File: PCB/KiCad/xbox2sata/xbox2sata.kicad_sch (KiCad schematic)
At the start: 43 parts, among them IC1 TLV1117LV12DCYR, J1 61203921621, J2 67800-8025, J3 90151-2140, U1 88SA8052, Y1 ABLS-25.000MHZ-B4-F-T

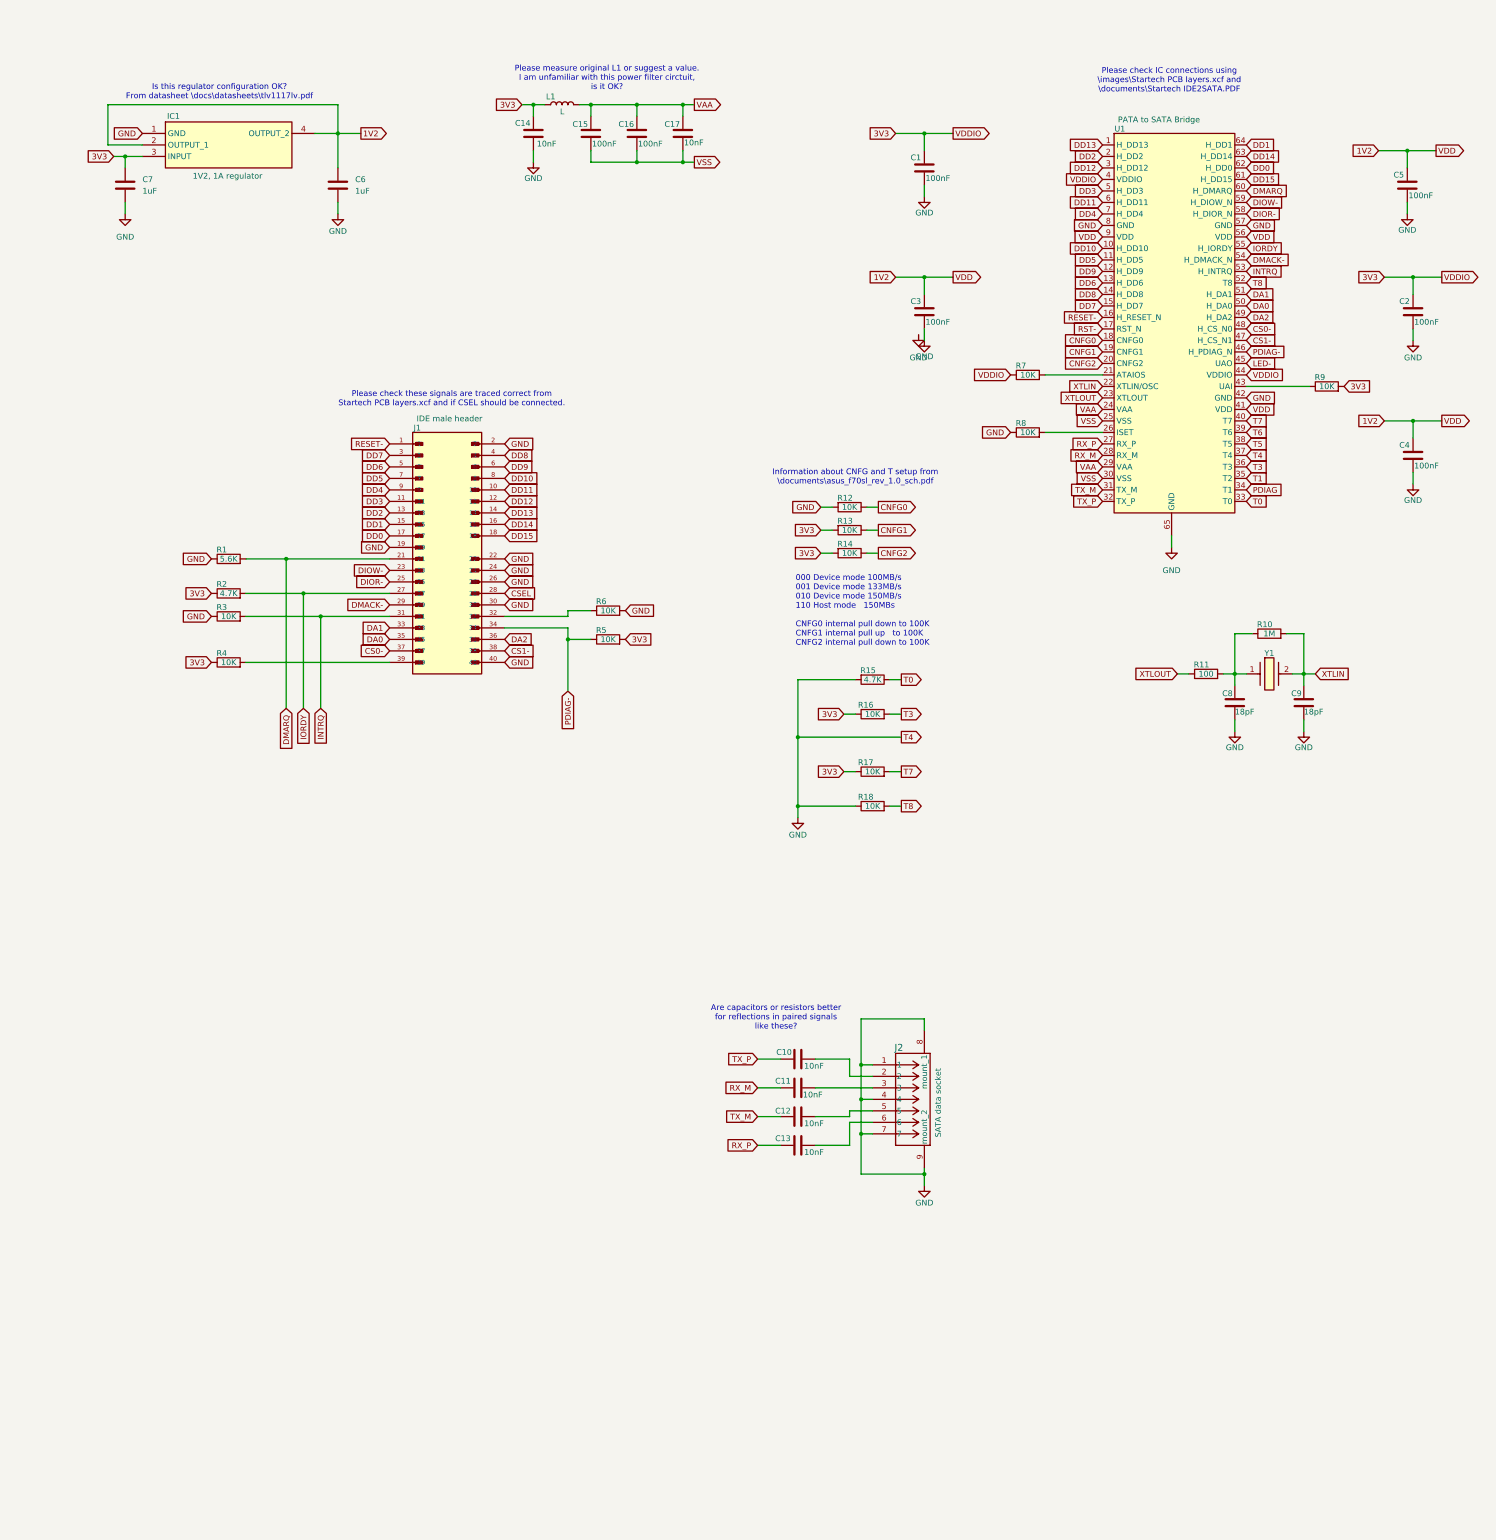
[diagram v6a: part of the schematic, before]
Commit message: 1V2 regulator circuit corrected, all labels need correcting
1V2 regulator circuit corrected, all labels need correcting
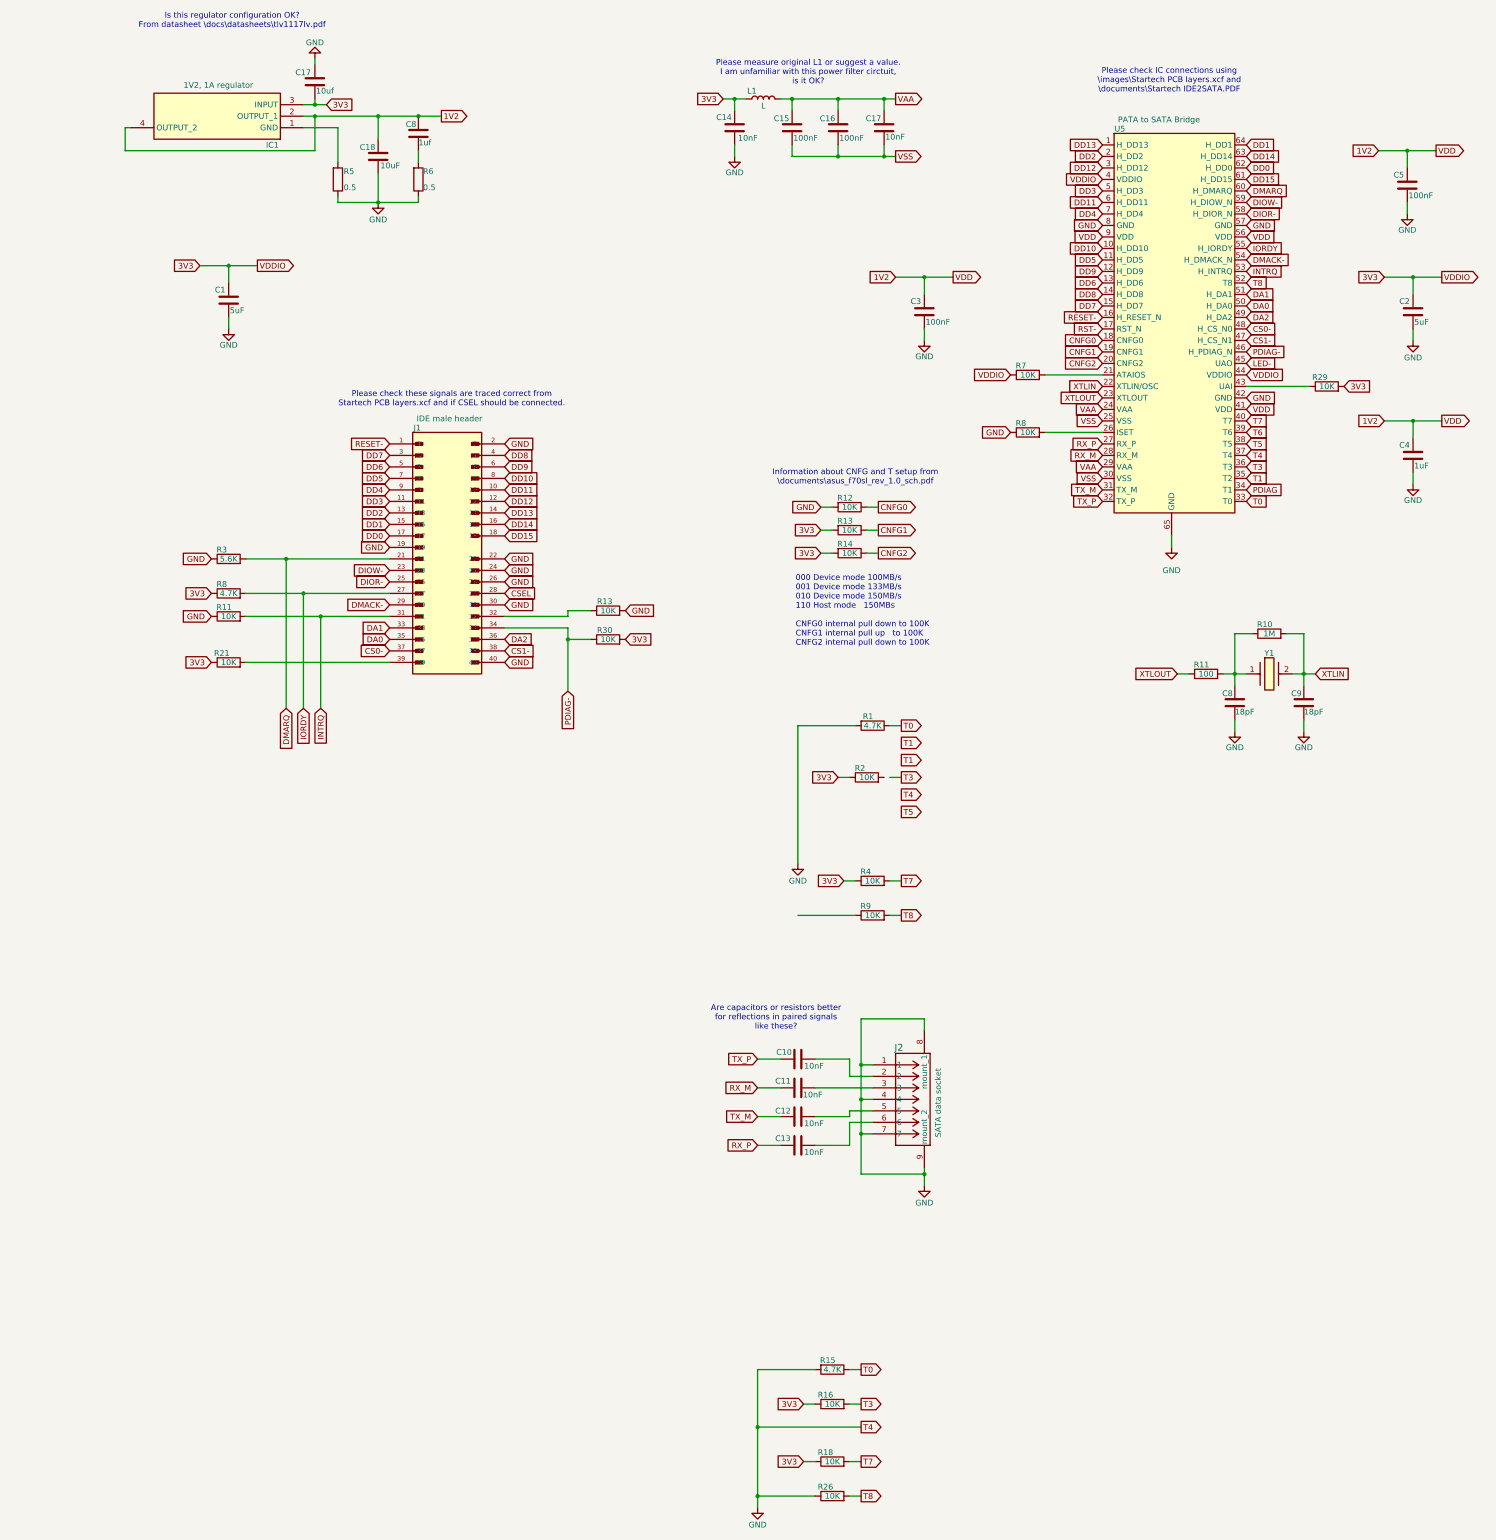
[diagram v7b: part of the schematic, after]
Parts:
- added C8: 1uf, symbol Device:C
- added R1: 4.7K, Resistor_SMD:R_0402_1005Metric_Pad0.72x0.64mm_HandSolder, symbol Device:R
- added R2, R4, R9: 10K, Resistor_SMD:R_0402_1005Metric_Pad0.72x0.64mm_HandSolder, symbol Device:R
- added R5, R6: 0.5, symbol Device:R
- C1, C2: value 100nF -> 5uF
- C17: renamed from C7; value 1uF -> 10uf
- C18: renamed from C6; value 1uF -> 10uF
- C4: value 100nF -> 1uF
- renumbered R3 to R11, R6 to R13, R17 to R18, R4 to R21, R18 to R26, R9 to R29, R1 to R3, R5 to R30, R2 to R8, U1 to U5
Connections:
- net 1V2: now also C8.2
- net 3V3: now also R2.1, R4.1
- net GND: now also R1.2, R5.1, R6.1; no longer IC1.1 (GND)
- net T0: now also R1.1
- net T7: now also R4.2
- net T8: now also R9.2
- new net: C8.1, R6.2
- new net: IC1.1 (GND), R5.2
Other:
- moved on the sheet: C1, C14, C15, C16, C17, C18, IC1, L1, R15, R16, R18, R26

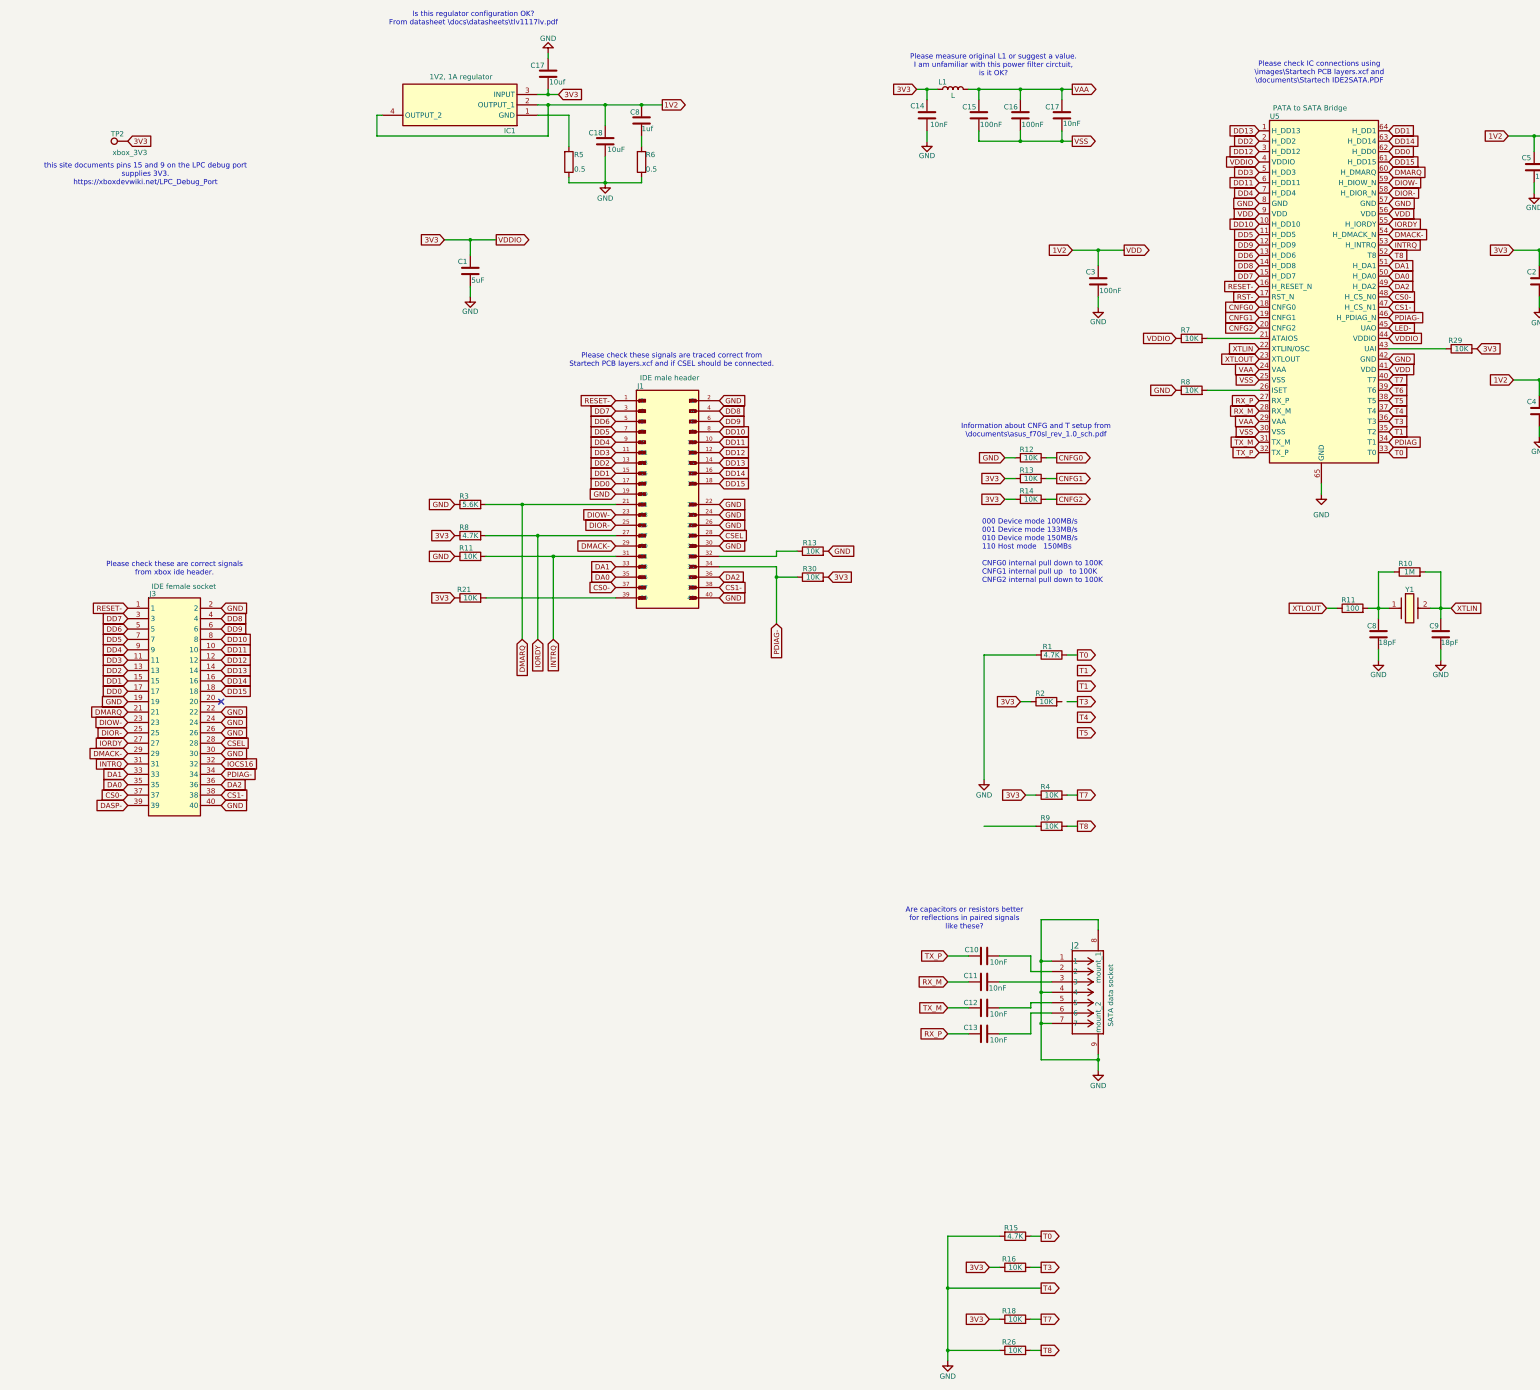
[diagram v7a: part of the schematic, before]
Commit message: T0-8 updated, label changes
Several cap and res labels changed, T0-8 config changed, layers.xcf saved with compression.
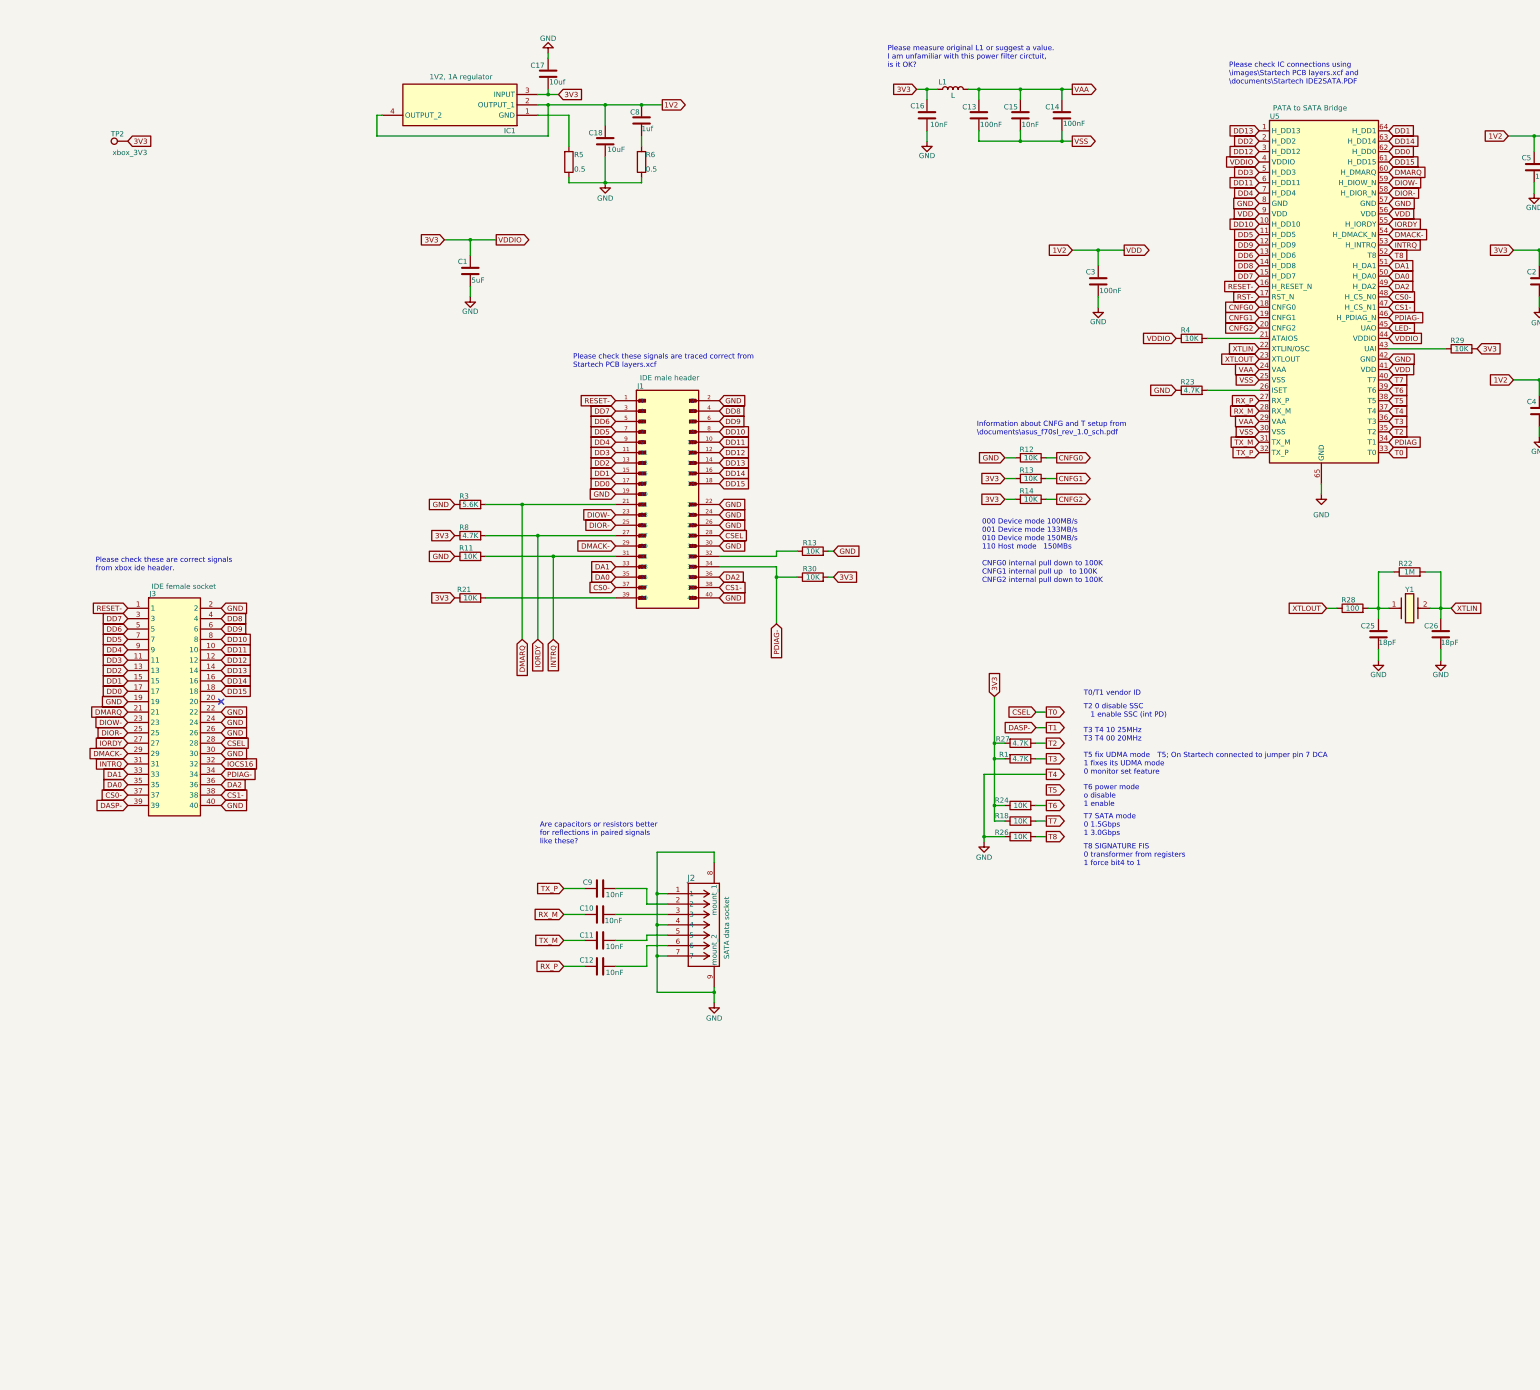
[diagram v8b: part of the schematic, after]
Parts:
- removed R15: 4.7K, Resistor_SMD:R_0402_1005Metric_Pad0.72x0.64mm_HandSolder, symbol Device:R
- removed R16, R18, R26: 10K, Resistor_SMD:R_0402_1005Metric_Pad0.72x0.64mm_HandSolder, symbol Device:R
- added R27: 4.7K, Resistor_SMD:R_0402_1005Metric_Pad0.72x0.64mm_HandSolder, symbol Device:R
- C14: renamed from C17; value 10nF -> 100nF
- C15: renamed from C16; value 100nF -> 10nF
- R23: renamed from R8; value 10K -> 4.7K
- renumbered C11 to C10, C12 to C11, C13 to C12, C15 to C13, C14 to C16, C8 to C25, C9 to C26, C10 to C9, R2 to R18, R10 to R22, R4 to R24, R9 to R26, R11 to R28, R7 to R4
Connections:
- net 3V3: now also R1.2, R27.2
- net CSEL: now also U5.33 (T0)
- net GND: now also R26.1; no longer R1.2
- net T3: now also R1.1
- net T6: now also R24.2
- net T7: now also R18.2; no longer R24.2
- removed net T0: R1.1, U5.33 (T0)
- net T1 renamed T2
- net T2: now also R27.1
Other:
- note added: "Please check these signals are traced correct from Startech PCB layers.xcf"
- note added: "T0/T1 vendor ID"
- note added: "T2 0 disable SSC 1 enable SSC (int PD)"
- note added: "T3 T4 10 25MHz T3 T4 00 20MHz"
- note added: "T5 fix UDMA mode 1 fixes its UDMA mode 0 monitor set feature"
- note added: "T5; On Startech connected to jumper pin 7 DCA"
- note added: "T6 power mode o disable 1 enable"
- note added: "T7 SATA mode 0 1.5Gbps 1 3.0Gbps"
- note added: "T8 SIGNATURE FIS 0 transformer from registers 1 force bit4 to 1"
- note removed: "Is this regulator configuration OK? From datasheet \docs\datasheets\tlv1117lv.pdf"
- note removed: "Please check these signals are traced correct from Startech PCB layers.xcf and if CSEL should be connected."
- note removed: "this site documents pins 15 and 9 on the LPC debug port supplies 3V3. https://xboxdevwiki.net/LPC_Debug_Port"
- moved on the sheet: C10, C11, C12, C9, J2, R1, R18, R24, R26
